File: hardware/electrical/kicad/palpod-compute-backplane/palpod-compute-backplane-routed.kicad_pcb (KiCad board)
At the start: 14 copper layers, 450 x 300 mm, 40 parts, among them J1 MM70_260_SODIMM (Jetson Orin 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, J10 MM70_260_SODIMM (Jetson Orin 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, J11 SAMTEC_EXAMAX_200 (Ryzen AI 9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, J12 SAMTEC_EXAMAX_200 (Ryzen AI 9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, J13 SAMTEC_EXAMAX_200 (Ryzen AI 9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, J14 SAMTEC_EXAMAX_200 (Ryzen AI 9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, J15 SAMTEC_EXAMAX_200 (Ryzen AI 9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, J16 SAMTEC_EXAMAX_200 (Ryzen AI 9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, J17 SAMTEC_EXAMAX_200 (Ryzen AI 9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, J18 SAMTEC_EXAMAX_200 (Ryzen AI 9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, J19 SAMTEC_EXAMAX_200 (Ryzen AI 9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, J2 MM70_260_SODIMM (Jetson Orin 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, J20 SAMTEC_EXAMAX_200 (Ryzen AI 9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, J21 ATX24 (+12V PSU input), J22 ATX24 (+12V PSU input B), J3 MM70_260_SODIMM (Jetson Orin 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, J4 MM70_260_SODIMM (Jetson Orin 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, J5 MM70_260_SODIMM (Jetson Orin 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, J6 MM70_260_SODIMM (Jetson Orin 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, J7 MM70_260_SODIMM (Jetson Orin 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, J8 MM70_260_SODIMM (Jetson Orin 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, J9 MM70_260_SODIMM (Jetson Orin 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, U1 BCM56780 (Trident 4 12.8Tbps), U2 ARIES_PT4 (PCIe Gen5 retimer), U3 UCD90320 (32-rail sequencer), U4 NCT6116 (BMC / super-I/O), U5 SLB9670 (TPM 2.0), U6 TPS543x (12V -> 5V, 15A)

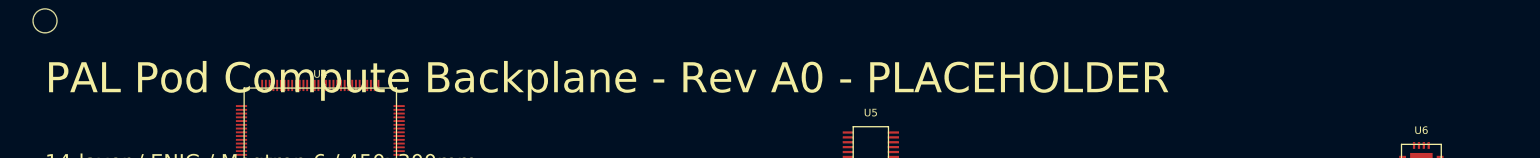
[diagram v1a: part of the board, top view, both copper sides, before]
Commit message: brand: broad KiCad sweep — remaining PAL Pod strings → Hearth
Targeted-pattern sed in ff14a48 missed variants. Broad find-replace
on .kicad_sch/pcb/pro/sym/mod + fp-lib-table + sym-lib-table +
per-project README.md (only where PAL Pod string actually appeared).
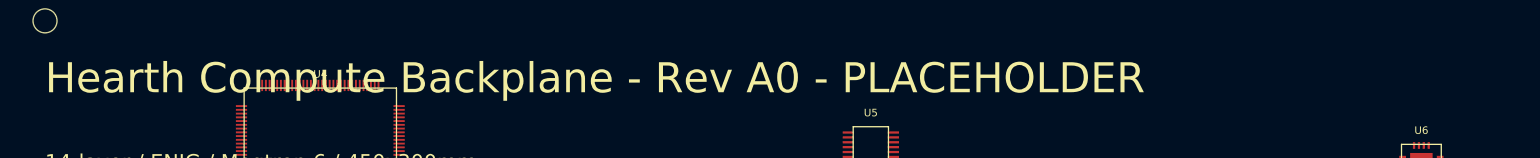
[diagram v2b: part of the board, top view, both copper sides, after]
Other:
- board text added: "Hearth Compute Backplane - Rev A0 - PLACEHOLDER"
- board text removed: "PAL Pod Compute Backplane - Rev A0 - PLACEHOLDER"
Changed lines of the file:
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@@
 	(paper "A2")
 	(title_block
-		(title "PAL Pod Compute Backplane - PCB")
+		(title "Hearth Compute Backplane - PCB")
 		(date "2026-08-03")
 		(rev "A0")
@@
 		)
 	)
-	(gr_text "PAL Pod Compute Backplane - Rev A0 - PLACEHOLDER"
+	(gr_text "Hearth Compute Backplane - Rev A0 - PLACEHOLDER"
 		(at 225 20 0)
 		(layer "F.SilkS")
